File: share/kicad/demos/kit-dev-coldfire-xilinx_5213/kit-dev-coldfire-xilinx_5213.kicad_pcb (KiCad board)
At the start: 4 copper layers, 157.5 x 91.4 mm, 162 parts, among them J1 JACK_2P, P1 CONN_6, P3 CONN_2X2, P4 CONN_20X2, Q1 3906, SW1 SW_PUSH, SW2 SW_PUSH, U1 MCF5213-LQFP100, U2 74AHC1G14, U3 MAX202, U4 74HC125, U5 MAX202, U7 PCA82C251, U8 MAX202, U9 XCR3256-TQ144, Y1 8MHz

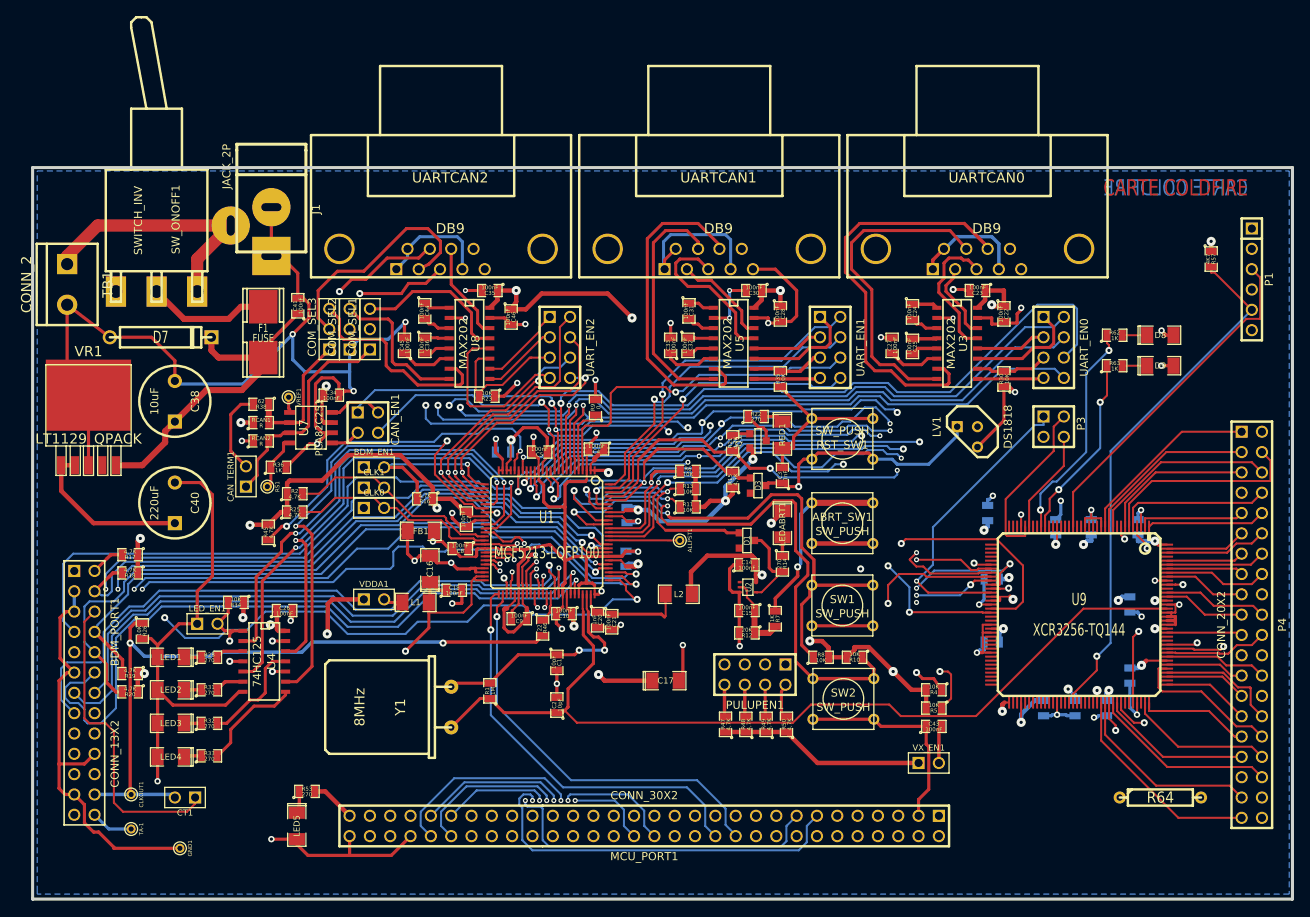
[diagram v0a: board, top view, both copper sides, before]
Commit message: Remove KiCad V4.0.7
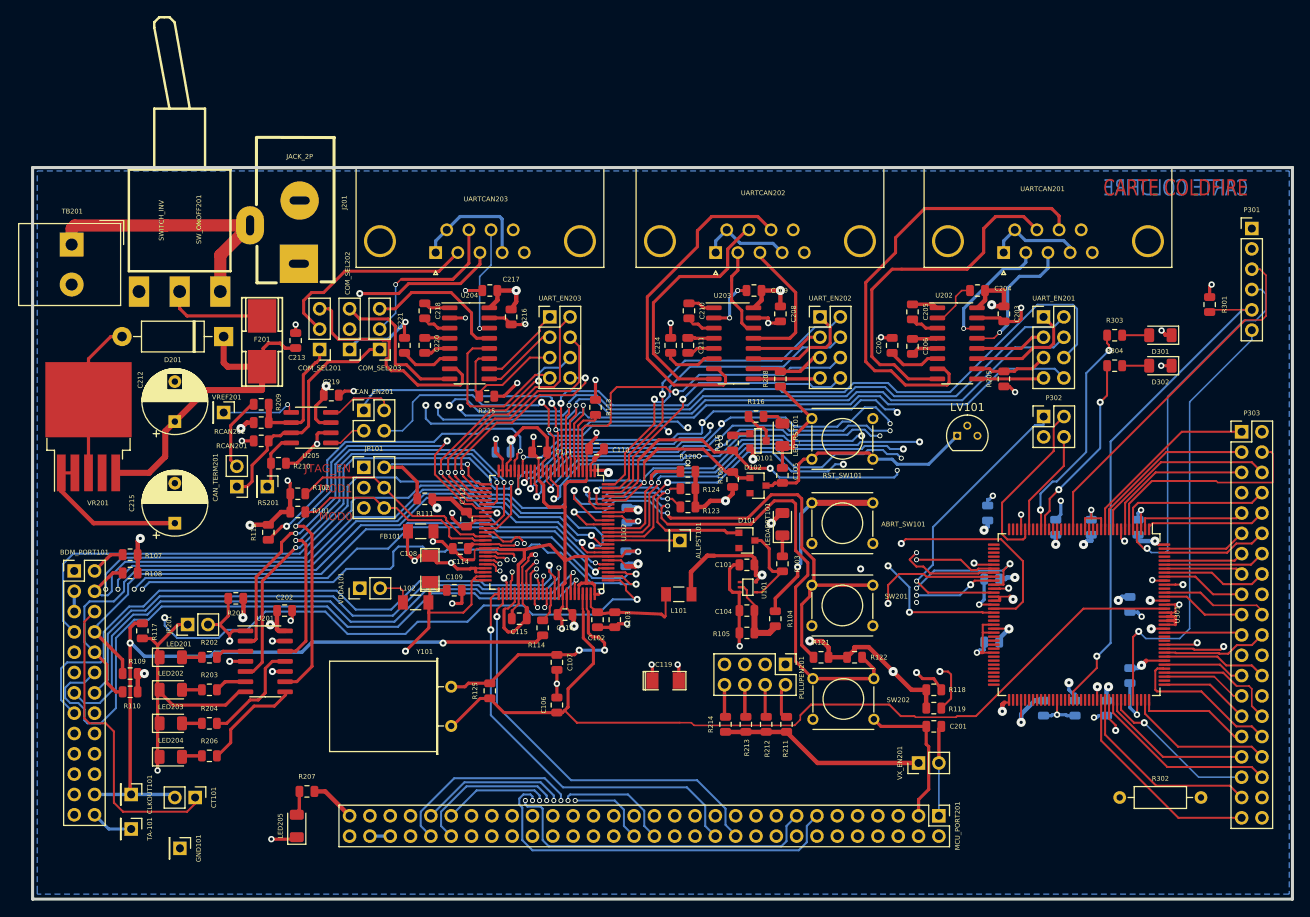
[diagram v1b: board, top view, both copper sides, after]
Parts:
- removed BDM_EN1, CLK0, CLK1, LED_EN1, VX_EN1: JUMPER, pin_array:PIN_ARRAY_2X1
- removed CAN_EN1, P3: CONN_2X2, pin_array:PIN_ARRAY_2X2
- removed COM_SEL3: CONN_3, pin_array:PIN_ARRAY_3X1
- removed U4: 74HC125, lib_smd:SO14E
- removed U9: XCR3256-TQ144, lib_smd:TQFP144
- removed UARTCAN0, UARTCAN1, UARTCAN2: DB9, connect:DB9FC
- removed VREF1: CONN_1, connect:PINTST
- added CAN_EN201: CONN_2X2, Connector_PinHeader_2.54mm:PinHeader_2x02_P2.54mm_Vertical, F.Cu at (112.5, 86.2)
- added COM_SEL201: CONN_3, Connector_PinHeader_2.54mm:PinHeader_1x03_P2.54mm_Vertical, F.Cu at (107.0, 78.6)
- added JP101: JUMPER_TRIPLE, Connector_PinHeader_2.54mm:PinHeader_2x03_P2.54mm_Vertical, F.Cu at (112.5, 93.3)
- added JP201: JUMPER, Connector_PinHeader_2.54mm:PinHeader_1x02_P2.54mm_Vertical, F.Cu at (90.5, 113.0)
- added P302: CONN_2X2, Connector_PinHeader_2.54mm:PinHeader_2x02_P2.54mm_Vertical, F.Cu at (197.5, 87.0)
- added U201: 74HC125, Package_SO:SOIC-14_3.9x8.7mm_P1.27mm, F.Cu at (100.2, 117.6)
- added U301: XCR3256-TQ144, Package_QFP:TQFP-144_20x20mm_P0.5mm, F.Cu at (201.9, 111.8)
- added UARTCAN201: DB9, Connector_Dsub:DSUB-9_Female_Horizontal_P2.77x2.84mm_EdgePinOffset7.70mm_Housed_MountingHolesOffset9.12mm, F.Cu at (192.5, 66.5)
- added UARTCAN202: DB9, Connector_Dsub:DSUB-9_Female_Horizontal_P2.77x2.84mm_EdgePinOffset7.70mm_Housed_MountingHolesOffset9.12mm, F.Cu at (156.5, 66.5)
- added UARTCAN203: DB9, Connector_Dsub:DSUB-9_Female_Horizontal_P2.77x2.84mm_EdgePinOffset7.70mm_Housed_MountingHolesOffset9.12mm, F.Cu at (121.5, 66.5)
- added VREF201: CONN_1, Connector_PinHeader_2.54mm:PinHeader_1x01_P2.54mm_Vertical, F.Cu at (95.0, 86.5)
- added VX_EN201: JUMPER, Connector_PinHeader_2.54mm:PinHeader_1x02_P2.54mm_Vertical, F.Cu at (181.9, 130.3)
- ABRT_SW101: renamed from ABRT_SW1; footprint discret:SW_PUSH_SMALL -> kit-dev-coldfire:SW_PUSH_SMALL
- ALLPST101: renamed from ALLPST1; footprint connect:PINTST -> Connector_PinHeader_2.54mm:PinHeader_1x01_P2.54mm_Vertical
- BDM_PORT101: renamed from BDM_PORT1; footprint pin_array:pin_array_13x2 -> Connector_PinHeader_2.54mm:PinHeader_2x13_P2.54mm_Vertical
- C101: renamed from C14; footprint lib_smd:SM0805 -> Capacitor_SMD:C_0805_2012Metric
- C102: renamed from C20; footprint lib_smd:SM0805 -> Capacitor_SMD:C_0805_2012Metric
- C103: renamed from C21; footprint lib_smd:SM0805 -> Capacitor_SMD:C_0805_2012Metric
- C104: renamed from C15; footprint lib_smd:SM0805 -> Capacitor_SMD:C_0805_2012Metric
- C105: renamed from C3; footprint lib_smd:SM0805 -> Capacitor_SMD:C_0805_2012Metric
- C106: renamed from C2; footprint lib_smd:SM0805 -> Capacitor_SMD:C_0805_2012Metric
- C107: renamed from C1; footprint lib_smd:SM0805 -> Capacitor_SMD:C_0805_2012Metric
- C108: renamed from C16; footprint lib_smd:SM1206POL -> kit-dev-coldfire:SM1206POL
- C109: renamed from C18; footprint lib_smd:SM0805 -> Capacitor_SMD:C_0805_2012Metric
- C110: renamed from C4; footprint lib_smd:SM0805 -> Capacitor_SMD:C_0805_2012Metric
- C111: renamed from C5; footprint lib_smd:SM0805 -> Capacitor_SMD:C_0805_2012Metric
- C112: renamed from C6; footprint lib_smd:SM0805 -> Capacitor_SMD:C_0805_2012Metric
- C113: renamed from C7; footprint lib_smd:SM0805 -> Capacitor_SMD:C_0805_2012Metric
- C114: renamed from C8; footprint lib_smd:SM0805 -> Capacitor_SMD:C_0805_2012Metric
- C115: renamed from C9; footprint lib_smd:SM0805 -> Capacitor_SMD:C_0805_2012Metric
- C116: renamed from C10; footprint lib_smd:SM0805 -> Capacitor_SMD:C_0805_2012Metric
- C117: renamed from C11; footprint lib_smd:SM0805 -> Capacitor_SMD:C_0805_2012Metric
- C118: renamed from C12; footprint lib_smd:SM0805 -> Capacitor_SMD:C_0805_2012Metric
- C119: renamed from C17; footprint lib_smd:SM1206POL -> kit-dev-coldfire:SM1206POL
- C201: renamed from C43; footprint lib_smd:SM0805 -> Capacitor_SMD:C_0805_2012Metric
- C202: renamed from C26; footprint lib_smd:SM0805 -> Capacitor_SMD:C_0805_2012Metric
- C203: renamed from C22; footprint lib_smd:SM0805 -> Capacitor_SMD:C_0805_2012Metric
- C204: renamed from C23; footprint lib_smd:SM0805 -> Capacitor_SMD:C_0805_2012Metric
- C205: renamed from C24; footprint lib_smd:SM0805 -> Capacitor_SMD:C_0805_2012Metric
- C206: renamed from C25; footprint lib_smd:SM0805 -> Capacitor_SMD:C_0805_2012Metric
- C207: renamed from C27; footprint lib_smd:SM0805 -> Capacitor_SMD:C_0805_2012Metric
- C208: renamed from C28; footprint lib_smd:SM0805 -> Capacitor_SMD:C_0805_2012Metric
- C209: renamed from C30; footprint lib_smd:SM0805 -> Capacitor_SMD:C_0805_2012Metric
- C210: renamed from C31; footprint lib_smd:SM0805 -> Capacitor_SMD:C_0805_2012Metric
- C211: renamed from C32; footprint lib_smd:SM0805 -> Capacitor_SMD:C_0805_2012Metric
- C212: renamed from C38; footprint discret:C2V8 -> Capacitor_THT:CP_Radial_D8.0mm_P5.00mm
- C213: renamed from C41; footprint lib_smd:SM0805 -> Capacitor_SMD:C_0805_2012Metric
- C214: renamed from C33; footprint lib_smd:SM0805 -> Capacitor_SMD:C_0805_2012Metric
- C215: renamed from C40; footprint discret:C2V8 -> Capacitor_THT:CP_Radial_D8.0mm_P5.00mm
- C216: renamed from C46; footprint lib_smd:SM0805 -> Capacitor_SMD:C_0805_2012Metric
- C217: renamed from C35; footprint lib_smd:SM0805 -> Capacitor_SMD:C_0805_2012Metric
- C218: renamed from C44; footprint lib_smd:SM0805 -> Capacitor_SMD:C_0805_2012Metric
- C219: renamed from C34; footprint lib_smd:SM0805 -> Capacitor_SMD:C_0805_2012Metric
- C220: renamed from C36; footprint lib_smd:SM0805 -> Capacitor_SMD:C_0805_2012Metric
- C221: renamed from C45; footprint lib_smd:SM0805 -> Capacitor_SMD:C_0805_2012Metric
- C301: renamed from C51; footprint lib_smd:SM0805 -> Capacitor_SMD:C_0805_2012Metric
- C302: renamed from C52; footprint lib_smd:SM0805 -> Capacitor_SMD:C_0805_2012Metric
- C303: renamed from C53; footprint lib_smd:SM0805 -> Capacitor_SMD:C_0805_2012Metric
- C304: renamed from C54; footprint lib_smd:SM0805 -> Capacitor_SMD:C_0805_2012Metric
- C305: renamed from C55; footprint lib_smd:SM0805 -> Capacitor_SMD:C_0805_2012Metric
- C306: renamed from C56; footprint lib_smd:SM0805 -> Capacitor_SMD:C_0805_2012Metric
- C307: renamed from C57; footprint lib_smd:SM0805 -> Capacitor_SMD:C_0805_2012Metric
- C308: renamed from C58; footprint lib_smd:SM0805 -> Capacitor_SMD:C_0805_2012Metric
- C309: renamed from C59; footprint lib_smd:SM0805 -> Capacitor_SMD:C_0805_2012Metric
- C310: renamed from C60; footprint lib_smd:SM0805 -> Capacitor_SMD:C_0805_2012Metric
- C311: renamed from C61; footprint lib_smd:SM0805 -> Capacitor_SMD:C_0805_2012Metric
- CAN_TERM201: renamed from CAN_TERM1; footprint pin_array:PIN_ARRAY_2X1 -> Connector_PinHeader_2.54mm:PinHeader_1x02_P2.54mm_Vertical
- CLKOUT101: renamed from CLKOUT1; footprint connect:PINTST -> Connector_PinHeader_2.54mm:PinHeader_1x01_P2.54mm_Vertical
- COM_SEL202: renamed from COM_SEL2; footprint pin_array:PIN_ARRAY_3X1 -> Connector_PinHeader_2.54mm:PinHeader_1x03_P2.54mm_Vertical
- COM_SEL203: renamed from COM_SEL1; footprint pin_array:PIN_ARRAY_3X1 -> Connector_PinHeader_2.54mm:PinHeader_1x03_P2.54mm_Vertical
- CT101: renamed from CT1; footprint pin_array:PIN_ARRAY_2X1 -> Connector_PinHeader_2.54mm:PinHeader_1x02_P2.54mm_Vertical
- D101: renamed from D1; footprint lib_smd:ST23AK#1 -> Diode_SMD:D_SOT-23_ANK
- D102: renamed from D3; footprint lib_smd:ST23AK#1 -> Diode_SMD:D_SOT-23_ANK
- D201: renamed from D7; footprint discret:D5 -> Diode_THT:D_DO-15_P12.70mm_Horizontal
- D301: renamed from D8; footprint lib_smd:SM1206POL -> LED_SMD:LED_1206_3216Metric
- D302: renamed from D9; footprint lib_smd:SM1206POL -> LED_SMD:LED_1206_3216Metric
- F201: renamed from F1; footprint lib_smd:FSUPCMS -> kit-dev-coldfire:FSUPCMS
- FB101: renamed from FB1; footprint lib_smd:SM1206 -> Resistor_SMD:R_1206_3216Metric_Pad1.24x1.80mm_HandSolder
- GND101: renamed from GND1; footprint connect:PINTST -> Connector_PinHeader_2.54mm:PinHeader_1x01_P2.54mm_Vertical
- J201: renamed from J1; footprint connect:JACK_ALIM -> kit-dev-coldfire:JACK_ALIM
- L101: renamed from L2; footprint lib_smd:SM1206 -> Resistor_SMD:R_1206_3216Metric_Pad1.24x1.80mm_HandSolder
- L102: renamed from L1; footprint lib_smd:SM1206 -> Resistor_SMD:R_1206_3216Metric_Pad1.24x1.80mm_HandSolder
- LED201: renamed from LED1; footprint lib_smd:SM1206POL -> LED_SMD:LED_1206_3216Metric
- LED202: renamed from LED2; footprint lib_smd:SM1206POL -> LED_SMD:LED_1206_3216Metric
- LED203: renamed from LED3; footprint lib_smd:SM1206POL -> LED_SMD:LED_1206_3216Metric
- LED204: renamed from LED4; footprint lib_smd:SM1206POL -> LED_SMD:LED_1206_3216Metric
- LED205: renamed from LED5; footprint lib_smd:SM1206POL -> LED_SMD:LED_1206_3216Metric
- LEDABRT101: renamed from LEDABRT1; value RED -> LED_RED; footprint lib_smd:SM1206POL -> LED_SMD:LED_1206_3216Metric
- LED_RST101: renamed from RED1; value LED_RESET1 -> LED_RED; footprint lib_smd:SM1206POL -> LED_SMD:LED_1206_3216Metric
- LV101: renamed from LV1; footprint discret:TO92-INVERT -> Package_TO_SOT_THT:TO-92_Molded_Narrow
- MCU_PORT201: renamed from MCU_PORT1; footprint pin_array:PIN_ARRAY_30X2 -> Connector_PinHeader_2.54mm:PinHeader_2x30_P2.54mm_Vertical
- P301: renamed from P1; footprint pin_array:PIN_ARRAY-6X1 -> Connector_PinHeader_2.54mm:PinHeader_1x06_P2.54mm_Vertical
- P303: renamed from P4; footprint pin_array:PIN_ARRAY_20X2 -> Connector_PinHeader_2.54mm:PinHeader_2x20_P2.54mm_Vertical
- PULUPEN201: renamed from PULUPEN1; footprint pin_array:pin_array_4x2 -> Connector_PinHeader_2.54mm:PinHeader_2x04_P2.54mm_Vertical
- Q101: renamed from Q1; footprint lib_smd:SOT23EBC -> kit-dev-coldfire:SOT23EBC
- R101: renamed from R25; footprint lib_smd:SM0805 -> Resistor_SMD:R_0805_2012Metric
- R102: renamed from R2; footprint lib_smd:SM0805 -> Resistor_SMD:R_0805_2012Metric
- R103: renamed from R14; footprint lib_smd:SM0805 -> Resistor_SMD:R_0805_2012Metric
- R104: renamed from R7; footprint lib_smd:SM0805 -> Resistor_SMD:R_0805_2012Metric
- R105: renamed from R12; footprint lib_smd:SM0805 -> Resistor_SMD:R_0805_2012Metric
- R106: renamed from R15; footprint lib_smd:SM0805 -> Resistor_SMD:R_0805_2012Metric
- R107: renamed from R17; footprint lib_smd:SM0805 -> Resistor_SMD:R_0805_2012Metric
- R108: renamed from R18; footprint lib_smd:SM0805 -> Resistor_SMD:R_0805_2012Metric
- R109: renamed from R19; footprint lib_smd:SM0805 -> Resistor_SMD:R_0805_2012Metric
- R110: renamed from R20; footprint lib_smd:SM0805 -> Resistor_SMD:R_0805_2012Metric
- R111: renamed from R16; footprint lib_smd:SM0805 -> Resistor_SMD:R_0805_2012Metric
- R112: renamed from R45; footprint lib_smd:SM0805 -> Resistor_SMD:R_0805_2012Metric
- R113: renamed from R9; footprint lib_smd:SM0805 -> Resistor_SMD:R_0805_2012Metric
- R114: renamed from R46; footprint lib_smd:SM0805 -> Resistor_SMD:R_0805_2012Metric
- R115: renamed from R21; value 4,7K -> 4.7K; footprint lib_smd:SM0805 -> Resistor_SMD:R_0805_2012Metric
- R116: renamed from R22; footprint lib_smd:SM0805 -> Resistor_SMD:R_0805_2012Metric
- R117: renamed from R26; footprint lib_smd:SM0805 -> Resistor_SMD:R_0805_2012Metric
- R118: renamed from R4; footprint lib_smd:SM0805 -> Resistor_SMD:R_0805_2012Metric
- R119: renamed from R5; footprint lib_smd:SM0805 -> Resistor_SMD:R_0805_2012Metric
- R120: renamed from R6; footprint lib_smd:SM0805 -> Resistor_SMD:R_0805_2012Metric
- R121: renamed from R8; footprint lib_smd:SM0805 -> Resistor_SMD:R_0805_2012Metric
- R122: renamed from R10; footprint lib_smd:SM0805 -> Resistor_SMD:R_0805_2012Metric
- R123: renamed from R11; footprint lib_smd:SM0805 -> Resistor_SMD:R_0805_2012Metric
- R124: renamed from R13; footprint lib_smd:SM0805 -> Resistor_SMD:R_0805_2012Metric
- R125: renamed from R1; footprint lib_smd:SM0805 -> Resistor_SMD:R_0805_2012Metric
- R201: renamed from R34; footprint lib_smd:SM0805 -> Resistor_SMD:R_0805_2012Metric
- R202: renamed from R28; footprint lib_smd:SM0805 -> Resistor_SMD:R_0805_2012Metric
- R203: renamed from R31; footprint lib_smd:SM0805 -> Resistor_SMD:R_0805_2012Metric
- R204: renamed from R32; footprint lib_smd:SM0805 -> Resistor_SMD:R_0805_2012Metric
- R205: renamed from R30; footprint lib_smd:SM0805 -> Resistor_SMD:R_0805_2012Metric
- R206: renamed from R33; footprint lib_smd:SM0805 -> Resistor_SMD:R_0805_2012Metric
- R207: renamed from R53; footprint lib_smd:SM0805 -> Resistor_SMD:R_0805_2012Metric
- R208: renamed from R35; footprint lib_smd:SM0805 -> Resistor_SMD:R_0805_2012Metric
- R209: renamed from R38; footprint lib_smd:SM0805 -> Resistor_SMD:R_0805_2012Metric
- R210: renamed from R36; footprint lib_smd:SM0805 -> Resistor_SMD:R_0805_2012Metric
- R211: renamed from R50; footprint lib_smd:SM0805 -> Resistor_SMD:R_0805_2012Metric
- R212: renamed from R49; footprint lib_smd:SM0805 -> Resistor_SMD:R_0805_2012Metric
- R213: renamed from R48; footprint lib_smd:SM0805 -> Resistor_SMD:R_0805_2012Metric
- R214: renamed from R47; footprint lib_smd:SM0805 -> Resistor_SMD:R_0805_2012Metric
- R215: renamed from R23; footprint lib_smd:SM0805 -> Resistor_SMD:R_0805_2012Metric
- R301: renamed from R57; footprint lib_smd:SM0805 -> Resistor_SMD:R_0805_2012Metric
- R302: renamed from R64; footprint discret:R4 -> Resistor_THT:R_Axial_DIN0207_L6.3mm_D2.5mm_P10.16mm_Horizontal
- R303: renamed from R62; footprint lib_smd:SM0805 -> Resistor_SMD:R_0805_2012Metric
- R304: renamed from R63; footprint lib_smd:SM0805 -> Resistor_SMD:R_0805_2012Metric
- RCAN201: renamed from RCAN2; footprint lib_smd:SM0805 -> Resistor_SMD:R_0805_2012Metric
- RCAN202: renamed from RCAN1; footprint lib_smd:SM0805 -> Resistor_SMD:R_0805_2012Metric
- RS201: renamed from RS1; footprint connect:PINTST -> Connector_PinHeader_2.54mm:PinHeader_1x01_P2.54mm_Vertical
- RST_SW101: renamed from RST_SW1; footprint discret:SW_PUSH_SMALL -> kit-dev-coldfire:SW_PUSH_SMALL
- SW201: renamed from SW1; footprint discret:SW_PUSH_SMALL -> kit-dev-coldfire:SW_PUSH_SMALL
- SW202: renamed from SW2; footprint discret:SW_PUSH_SMALL -> kit-dev-coldfire:SW_PUSH_SMALL
- SW_ONOFF201: renamed from SW_ONOFF1; footprint discret:SW_SPDT -> kit-dev-coldfire:SW_SPDT
- TA-101: renamed from TA-1; footprint connect:PINTST -> Connector_PinHeader_2.54mm:PinHeader_1x01_P2.54mm_Vertical
- TB201: renamed from TB1; footprint connect:bornier2 -> TerminalBlock_Altech:Altech_AK300_1x02_P5.00mm_45-Degree
- U101: renamed from U2; footprint lib_smd:SOT353 -> kit-dev-coldfire:SOT353
- U102: renamed from U1; footprint lib_smd:VQFP100 -> Package_QFP:LQFP-100_14x14mm_P0.5mm
- U202: renamed from U3; footprint lib_smd:SO16E -> Package_SO:SOIC-16_3.9x9.9mm_P1.27mm
- U203: renamed from U5; footprint lib_smd:SO16E -> Package_SO:SOIC-16_3.9x9.9mm_P1.27mm
- U204: renamed from U8; footprint lib_smd:SO16E -> Package_SO:SOIC-16_3.9x9.9mm_P1.27mm
- U205: renamed from U7; footprint lib_smd:SO8E -> Package_SO:SOIC-8_3.9x4.9mm_P1.27mm
- UART_EN201: renamed from UART_EN0; footprint pin_array:pin_array_4x2 -> Connector_PinHeader_2.54mm:PinHeader_2x04_P2.54mm_Vertical
- UART_EN202: renamed from UART_EN1; footprint pin_array:pin_array_4x2 -> Connector_PinHeader_2.54mm:PinHeader_2x04_P2.54mm_Vertical
- UART_EN203: renamed from UART_EN2; footprint pin_array:pin_array_4x2 -> Connector_PinHeader_2.54mm:PinHeader_2x04_P2.54mm_Vertical
- VDDA101: renamed from VDDA1; footprint pin_array:PIN_ARRAY_2X1 -> Connector_PinHeader_2.54mm:PinHeader_1x02_P2.54mm_Vertical
- VR201: renamed from VR1; footprint lib_smd:DPAK5 -> Package_TO_SOT_SMD:TO-263-5_TabPin3
- Y101: renamed from Y1; footprint discret:HC-18UH -> Crystal:Crystal_HC18-U_Horizontal
- moved MCU_PORT201 36.9 mm to (184.4, 136.9), turned to -90 degrees
- moved P303 24.2 mm to (222.2, 88.9), turned to 0 degrees
- moved BDM_PORT101 15.3 mm to (76.3, 106.3), turned to 0 degrees
- moved D201 7.88 mm to (95.0, 77.0), turned to 180 degrees
- moved P301 6.35 mm to (223.5, 63.5), turned to 0 degrees
- moved R301 5.69 mm to (218.2, 73.0)
- moved R302 5.08 mm to (207.0, 134.6)
- moved TB201 5.02 mm to (76.0, 65.5)
- moved VR201 4.83 mm to (78.1, 88.3), turned to 90 degrees
- moved C213 4.36 mm to (104.0, 77.5)
- moved PULUPEN201 4.02 mm to (165.2, 118.0), turned to -90 degrees
- moved UART_EN202 4.02 mm to (169.5, 74.5), turned to 0 degrees
- moved UART_EN201 4.02 mm to (197.5, 74.5), turned to 0 degrees
- moved UART_EN203 4.02 mm to (135.8, 74.5), turned to 0 degrees
- moved J201 3.63 mm to (104.5, 60.0)
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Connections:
- net /CLKIN/EXTAL renamed /CLKIN/EXTAL
- net /inout_user/CANRX renamed /CANRX
- net /inout_user/CANTX renamed /CANTX
- net /inout_user/PWM1 renamed /PWM1
- net /inout_user/PWM3 renamed /PWM3
- net /inout_user/PWM5 renamed /PWM5
- net /inout_user/PWM7 renamed /PWM7
- net /inout_user/QSPI_DIN renamed /QSPI_DIN
- net /inout_user/QSPI_DOUT renamed /DSPI_DOUT
- net /inout_user/QSPI_SCLK renamed /QSPI_CLK
- net /inout_user/RCON- renamed /RCON-
- net /inout_user/RTS0- renamed /RSTO-
- net /inout_user/UCTS0 renamed /UCTS0
- net /inout_user/UCTS1 renamed /UCTS1
- net /inout_user/UCTS2 renamed /UCTS2
- net /inout_user/URTS0 renamed /URTS0
- net /inout_user/URTS1 renamed /URTS1
- net /inout_user/URTS2 renamed /URTS2
- net /inout_user/URXD0 renamed /URXD0
- net /inout_user/URXD1 renamed /URXD1
- net /inout_user/URXD2 renamed /URXD2
- net /inout_user/UTXD0 renamed /UTXD0
- net /inout_user/UTXD1 renamed /UTXD1
- net /inout_user/UTXD2 renamed /UTXD2
- net /inout_user/VCCA renamed /VCCA
- net /xilinx/GLCK2 renamed /XTAL
- net /xilinx/IRQ-1 renamed /IRQ-1
- net /xilinx/IRQ-2 renamed /IRQ-2
- net /xilinx/IRQ-3 renamed /IRQ-3
- net /xilinx/QSPI_CS1 renamed /QSPI_CS1
- net /xilinx/QSPI_CS2 renamed /QSPI_CS2
- ABRT_SW101 pad 2: VDD -> +3.3V
- BDM_PORT101 pad 1: (no net) -> unconnected-(BDM_PORT101-Pad1)
- BDM_PORT101 pad 21: (no net) -> unconnected-(BDM_PORT101-Pad21)
- BDM_PORT101 pad 22: (no net) -> unconnected-(BDM_PORT101-Pad22)
- BDM_PORT101 pad 25: VDD -> +3.3V
- BDM_PORT101 pad 7: /inout_user/RSTI- -> /RSTI-
- BDM_PORT101 pad 9: VDD -> +3.3V
- C101 pad 2: VDD -> +3.3V
- C105 pad 1: Net-(C3-Pad1) -> Net-(C105-Pad1)
- C110 pad 1: VDD -> +3.3V
- C111 pad 1: VDD -> +3.3V
- C112 pad 1: VDD -> +3.3V
- C113 pad 1: VDD -> +3.3V
- C114 pad 1: VDD -> +3.3V
- C115 pad 1: VDD -> +3.3V
- C116 pad 1: VDD -> +3.3V
- C117 pad 1: VDD -> +3.3V
- C118 pad 1: VDD -> +3.3V
- C119 pad 1: VDD -> +3.3V
- C202 pad 1: VDD -> +3.3V
- C203 pad 1: VDD -> +3.3V
- C204 pad 1: VDD -> +3.3V
- C208 pad 1: VDD -> +3.3V
- C209 pad 1: VDD -> +3.3V
- C212 pad 1: Net-(C38-Pad1) -> Net-(C212-Pad1)
- C213 pad 1: Net-(C38-Pad1) -> Net-(C212-Pad1)
- C215 pad 1: VDD -> +3.3V
- C216 pad 1: VDD -> +3.3V
- C217 pad 1: VDD -> +3.3V
- C219 pad 1: VDD -> +3.3V
- C301 pad 1: VDD -> +3.3V
- C302 pad 1: VDD -> +3.3V
- C303 pad 1: VDD -> +3.3V
- C304 pad 1: VDD -> +3.3V
- C305 pad 1: VDD -> +3.3V
- C306 pad 1: VDD -> +3.3V
- C307 pad 1: VDD -> +3.3V
- C308 pad 1: VDD -> +3.3V
- C309 pad 1: VDD -> +3.3V
- C310 pad 1: VDD -> +3.3V
- C311 pad 1: VDD -> +3.3V
- COM_SEL203 pad 2: /inout_user/CTS2/CANH -> /inout_user/CTS2/CANH
- D101 pad 1: /IRQ-7 -> Net-(D101-Pad1)
- D101 pad 2: Net-(D1-Pad2) -> /IRQ-7
- D102 pad 1: /inout_user/RSTI- -> Net-(C105-Pad1)
- D102 pad 2: Net-(C3-Pad1) -> /RSTI-
- D201 pad 1: GND -> Net-(C212-Pad1)
- D201 pad 2: Net-(C38-Pad1) -> GND
- D301 pad 1: Net-(D8-Pad1) -> GND
- D301 pad 2: GND -> Net-(D301-Pad2)
- D302 pad 1: Net-(D9-Pad1) -> GND
- D302 pad 2: GND -> Net-(D302-Pad2)
- F201 pad 2: Net-(C38-Pad1) -> Net-(C212-Pad1)
- L101 pad 1: VDD -> +3.3V
- LED201 pad 1: Net-(LED1-Pad1) -> GND
- LED201 pad 2: GND -> Net-(LED201-Pad2)
- LED202 pad 1: Net-(LED2-Pad1) -> GND
- LED202 pad 2: GND -> Net-(LED202-Pad2)
- LED203 pad 1: Net-(LED3-Pad1) -> GND
- LED203 pad 2: GND -> Net-(LED203-Pad2)
- LED204 pad 1: Net-(LED4-Pad1) -> GND
- LED204 pad 2: GND -> Net-(LED204-Pad2)
- LED205 pad 1: Net-(LED5-Pad1) -> GND
- LED205 pad 2: GND -> Net-(LED205-Pad2)
- LEDABRT101 pad 1: VDD -> Net-(LEDABRT101-Pad1)
- LEDABRT101 pad 2: Net-(LEDABRT1-Pad2) -> +3.3V
- LED_RST101 pad 1: Net-(R22-Pad2) -> GND
- LED_RST101 pad 2: GND -> Net-(LED_RST101-Pad2)
- LV101 pad 1: Net-(C3-Pad1) -> Net-(C105-Pad1)
- LV101 pad 2: VDD -> +3.3V
- MCU_PORT201 pad 59: VDD -> +3.3V
- MCU_PORT201 pad 6: /inout_user/RSTI- -> /RSTI-
- P301 pad 1: VDD -> +3.3V
- Q101 pad 1: VDD -> +3.3V
- R101 pad 1: VDD -> +3.3V
- R102 pad 1: VDD -> +3.3V
- R103 pad 1: Net-(LEDABRT1-Pad2) -> Net-(LEDABRT101-Pad1)
- R103 pad 2: Net-(D1-Pad2) -> Net-(D101-Pad1)
- R106 pad 1: VDD -> +3.3V
- R106 pad 2: /inout_user/RSTI- -> /RSTI-
- R107 pad 1: VDD -> +3.3V
- R108 pad 1: VDD -> +3.3V
- R109 pad 1: VDD -> +3.3V
- R110 pad 1: VDD -> +3.3V
- R111 pad 1: VDD -> +3.3V
- R112 pad 2: VDD -> +3.3V
- R116 pad 2: Net-(R22-Pad2) -> Net-(LED_RST101-Pad2)
- R118 pad 2: VDD -> +3.3V
- R119 pad 2: VDD -> +3.3V
- R120 pad 2: VDD -> +3.3V
- R121 pad 2: VDD -> +3.3V
- R122 pad 2: VDD -> +3.3V
- R123 pad 2: VDD -> +3.3V
- R124 pad 2: VDD -> +3.3V
- R201 pad 1: VDD -> +3.3V
- R202 pad 1: Net-(LED1-Pad1) -> Net-(LED201-Pad2)
- R203 pad 1: Net-(LED2-Pad1) -> Net-(LED202-Pad2)
- R204 pad 1: Net-(LED3-Pad1) -> Net-(LED203-Pad2)
- R206 pad 1: Net-(LED4-Pad1) -> Net-(LED204-Pad2)
- R207 pad 1: Net-(LED5-Pad1) -> Net-(LED205-Pad2)
- R207 pad 2: VDD -> +3.3V
- R211 pad 1: VDD -> +3.3V
- R212 pad 1: VDD -> +3.3V
- R213 pad 1: VDD -> +3.3V
- R214 pad 1: VDD -> +3.3V
- R301 pad 1: VDD -> +3.3V
- R302 pad 1: VDD -> +3.3V
- R303 pad 2: Net-(D8-Pad1) -> Net-(D301-Pad2)
- R304 pad 2: Net-(D9-Pad1) -> Net-(D302-Pad2)
- RCAN202 pad 1: VDD -> +3.3V
- RST_SW101 pad 1: Net-(C3-Pad1) -> Net-(C105-Pad1)
- SW_ONOFF201 pad 1: (no net) -> unconnected-(SW_ONOFF201-Pad1)
- U101 pad 4: Net-(D1-Pad2) -> Net-(D101-Pad1)
- U101 pad 5: VDD -> +3.3V
- U102 pad 1: VDD -> +3.3V
- U102 pad 14: VDD -> +3.3V
- U102 pad 2: VDD -> +3.3V
- U102 pad 22: VDD -> +3.3V
- U102 pad 23: VDD -> +3.3V
- U102 pad 34: VDD -> +3.3V
- U102 pad 41: VDD -> +3.3V
- U102 pad 55: VDD -> +3.3V
- U102 pad 57: VDD -> +3.3V
- U102 pad 68: VDD -> +3.3V
- U102 pad 81: VDD -> +3.3V
- U102 pad 93: VDD -> +3.3V
- U102 pad 96: /inout_user/RSTI- -> /RSTI-
- U202 pad 16: VDD -> +3.3V
- U203 pad 16: VDD -> +3.3V
- U204 pad 16: VDD -> +3.3V
- U205 pad 3: VDD -> +3.3V
- VDDA101 pad 1: VDD -> +3.3V
- VR201 pad 1: VDD -> +3.3V
- VR201 pad 2: VDD -> +3.3V
- VR201 pad 4: (no net) -> unconnected-(VR201-Pad4)
- VR201 pad 5: Net-(C38-Pad1) -> Net-(C212-Pad1)
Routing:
- net VDD: track 983.5 -> 0.00 mm, vias 44 -> 0
- net GND: track 1134.9 -> 347.3 mm
- net +3.3V: track 0.00 -> 308.4 mm, vias 0 -> 43
- net /RSTI-: track 0.00 -> 207.4 mm, vias 0 -> 2
- net /inout_user/RSTI-: track 207.4 -> 0.00 mm, vias 2 -> 0
- net Net-(C212-Pad1): track 0.00 -> 42.5 mm
- net Net-(C38-Pad1): track 41.5 -> 0.00 mm
- net Net-(C3-Pad1): track 31.0 -> 0.00 mm, vias 1 -> 0
- net /inout_user/TXD2/CANL: track 29.4 -> 0.00 mm
- net Net-(C105-Pad1): track 0.00 -> 28.9 mm
- net /inout_user/TXD2/CANL: track 0.00 -> 26.2 mm
- net /inout_user/CTS2/CANH: track 23.5 -> 0.00 mm, vias 1 -> 0
- net Net-(P302-Pad2): track 0.00 -> 22.1 mm
- net Net-(P3-Pad2): track 21.4 -> 0.00 mm
- net /inout_user/CTS2/CANH: track 0.00 -> 20.8 mm, vias 0 -> 1
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- added copper zone on In2.Cu, net +3.3V
- added copper zone on In1.Cu, net GND
- removed copper zone on GND_layer, net GND
- removed copper zone on VDD_layer, net VDD
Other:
- net class Default removed
- net class POWER removed
- rule pad_to_mask_clearance: 0.2 -> 0
- board text added: "JTAG_EN"
- board text added: "MOD0"
- board text added: "MOD1"
